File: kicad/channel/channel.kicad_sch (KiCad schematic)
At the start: 34 parts, among them J1 Conn_01x07_Male, J2 Conn_01x01_Male, J3 Conn_01x01_Male, J4 Conn_01x01_Male, J5 Conn_01x01_Male, Q1 BC846B, Q2 IRF3205, Q3 IRF3205, Q4 BC846B, Q5 IRF3205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

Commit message: work on kicad
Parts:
- removed C5, C6: 10u, Capacitor_SMD:CP_Elec_6.3x7.7, symbol Device:C_Polarized
- added C5, C6: 1u, Capacitor_SMD:C_0603_1608Metric, symbol Device:C
- added R17, R18: 10k, Resistor_SMD:R_1206_3216Metric, symbol Device:R
- added R19, R20: 2.2k, Resistor_SMD:R_1206_3216Metric, symbol Device:R
- R10, R11, R2, R3: value 47k -> 22k
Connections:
- net GND: now also R19.1, R20.1; no longer Q1.2 (E), Q4.2 (E)
- net at R1.2, U1.14: now also R18.1
- net at R2.2, R4.1, U1.9 (-): now also C5.1
- net at R9.2, U1.8: now also R17.1
- net at R10.2, R12.1, U1.13 (-): now also C6.1
- new net: C5.2, R17.2
- new net: Q1.2 (E), R19.2
- new net: C6.2, R18.2
- new net: Q4.2 (E), R20.2
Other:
- moved on the sheet: R1, R9, U1C, U1D

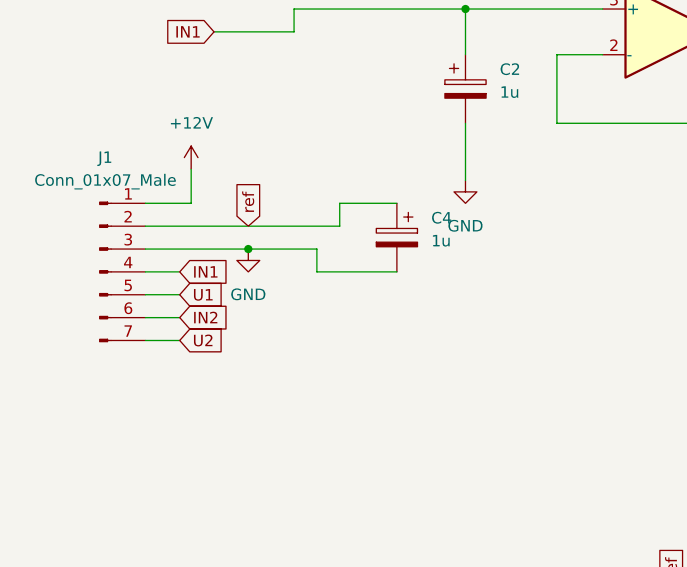
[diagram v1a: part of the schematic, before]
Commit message: rework PINS, get SD Card working
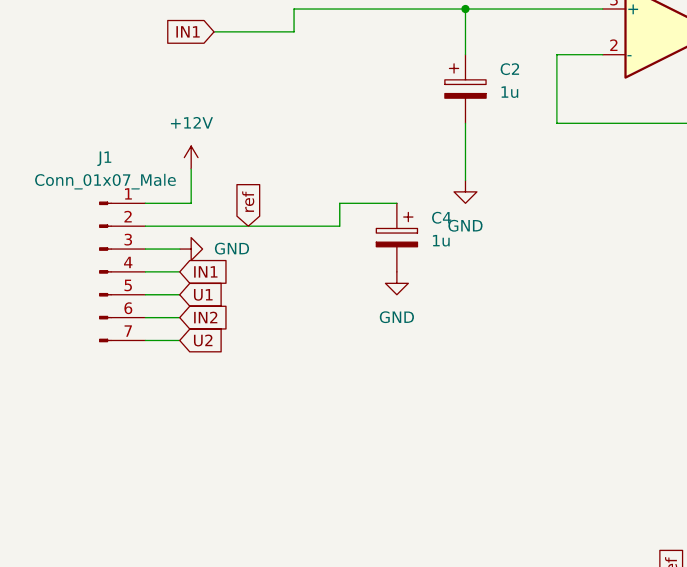
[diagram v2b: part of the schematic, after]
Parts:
- R8: footprint Resistor_THT:R_Axial_DIN0614_L14.3mm_D5.7mm_P25.40mm_Horizontal -> Resistor_THT:R_Axial_DIN0614_L14.3mm_D5.7mm_P20.32mm_Horizontal
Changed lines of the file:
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@@
   (junction (at 152.4 132.08) (diameter 0) (color 0 0 0 0)
   )
-  (junction (at 38.1 97.79) (diameter 0) (color 0 0 0 0)
-  )
   (junction (at 167.64 121.92) (diameter 0) (color 0 0 0 0)
   )
@@
     (stroke (width 0) (type default) (color 0 0 0 0))
   )
-  (wire (pts (xy 45.72 97.79) (xy 45.72 100.33))
-    (stroke (width 0) (type default) (color 0 0 0 0))
-  )
   (wire (pts (xy 153.67 83.82) (xy 153.67 87.63))
     (stroke (width 0) (type default) (color 0 0 0 0))
@@
     (stroke (width 0) (type default) (color 0 0 0 0))
   )
+  (wire (pts (xy 26.67 97.79) (xy 30.48 97.79))
+    (stroke (width 0) (type default) (color 0 0 0 0))
+  )
   (wire (pts (xy 124.46 132.08) (xy 130.81 132.08))
     (stroke (width 0) (type default) (color 0 0 0 0))
@@
     (stroke (width 0) (type default) (color 0 0 0 0))
   )
-  (wire (pts (xy 26.67 97.79) (xy 38.1 97.79))
-    (stroke (width 0) (type default) (color 0 0 0 0))
-  )
   (wire (pts (xy 111.76 144.78) (xy 114.3 144.78))
     (stroke (width 0) (type default) (color 0 0 0 0))
@@
     (stroke (width 0) (type default) (color 0 0 0 0))
   )
-  (wire (pts (xy 45.72 100.33) (xy 54.61 100.33))
-    (stroke (width 0) (type default) (color 0 0 0 0))
-  )
   (wire (pts (xy 54.61 92.71) (xy 48.26 92.71))
     (stroke (width 0) (type default) (color 0 0 0 0))
@@
   )
   (wire (pts (xy 201.93 73.66) (xy 129.54 73.66))
-    (stroke (width 0) (type default) (color 0 0 0 0))
-  )
-  (wire (pts (xy 38.1 97.79) (xy 45.72 97.79))
     (stroke (width 0) (type default) (color 0 0 0 0))
   )
@@
     (pin "1")
   )
+  (symbol (lib_id "power:GND") (at 30.48 97.79 90) (unit 1)
+    (in_bom yes) (on_board yes) (fields_autoplaced)
+    (property "Reference" "#PWR0105" (id 0) (at 36.83 97.79 0)
+      (effects (font (size 1.27 1.27)) hide)
+    )
+    (property "Value" "GND" (id 1) (at 34.29 97.7899 90)
+      (effects (font (size 1.27 1.27)) (justify right))
+    )
+    (property "Footprint" "" (id 2) (at 30.48 97.79 0)
+      (effects (font (size 1.27 1.27)) hide)
+    )
+    (property "Datasheet" "" (id 3) (at 30.48 97.79 0)
+      (effects (font (size 1.27 1.27)) hide)
+    )
+    (pin "1")
+  )
   (symbol (lib_id "power:GND") (at 154.94 163.83 0) (unit 1)
     (in_bom yes) (on_board yes) (fields_autoplaced)
@@
     (pin "2")
   )
-  (symbol (lib_id "power:GND") (at 38.1 97.79 0) (unit 1)
-    (in_bom yes) (on_board yes) (fields_autoplaced)
-    (property "Reference" "#PWR0103" (id 0) (at 38.1 104.14 0)
-      (effects (font (size 1.27 1.27)) hide)
-    )
-    (property "Value" "GND" (id 1) (at 38.1 102.87 0))
-    (property "Footprint" "" (id 2) (at 38.1 97.79 0)
-      (effects (font (size 1.27 1.27)) hide)
-    )
-    (property "Datasheet" "" (id 3) (at 38.1 97.79 0)
+  (symbol (lib_id "power:GND") (at 54.61 100.33 0) (unit 1)
+    (in_bom yes) (on_board yes) (fields_autoplaced)
+    (property "Reference" "#PWR0103" (id 0) (at 54.61 106.68 0)
+      (effects (font (size 1.27 1.27)) hide)
+    )
+    (property "Value" "GND" (id 1) (at 54.61 105.41 0))
+    (property "Footprint" "" (id 2) (at 54.61 100.33 0)
+      (effects (font (size 1.27 1.27)) hide)
+    )
+    (property "Datasheet" "" (id 3) (at 54.61 100.33 0)
       (effects (font (size 1.27 1.27)) hide)
     )
@@
     (property "Reference" "R8" (id 0) (at 182.88 115.57 90))
     (property "Value" "0.22" (id 1) (at 182.88 118.11 90))
-    (property "Footprint" "Resistor_THT:R_Axial_DIN0614_L14.3mm_D5.7mm_P25.40mm_Horizontal" (id 2) (at 182.88 123.698 90)
+    (property "Footprint" "Resistor_THT:R_Axial_DIN0614_L14.3mm_D5.7mm_P20.32mm_Horizontal" (id 2) (at 182.88 123.698 90)
       (effects (font (size 1.27 1.27)) hide)
     )
@@
       (reference "#PWR0104") (unit 1) (value "+12V") (footprint "")
     )
+    (path "/8a8f424c-3033-4534-9311-6e7b42dedc1f"
+      (reference "#PWR0105") (unit 1) (value "GND") (footprint "")
+    )
     (path "/98bcbe84-6de1-4d54-8e02-faa40f5f06a1"
       (reference "C1") (unit 1) (value "1u") (footprint "Capacitor_SMD:C_0603_1608Metric")
@@
     )
     (path "/c800057a-d278-4182-854b-774312f90617"
-      (reference "R8") (unit 1) (value "0.22") (footprint "Resistor_THT:R_Axial_DIN0614_L14.3mm_D5.7mm_P25.40mm_Horizontal")
+      (reference "R8") (unit 1) (value "0.22") (footprint "Resistor_THT:R_Axial_DIN0614_L14.3mm_D5.7mm_P20.32mm_Horizontal")
     )
     (path "/5f4f5dfc-c04c-423a-8bfb-e97fdc53c047"

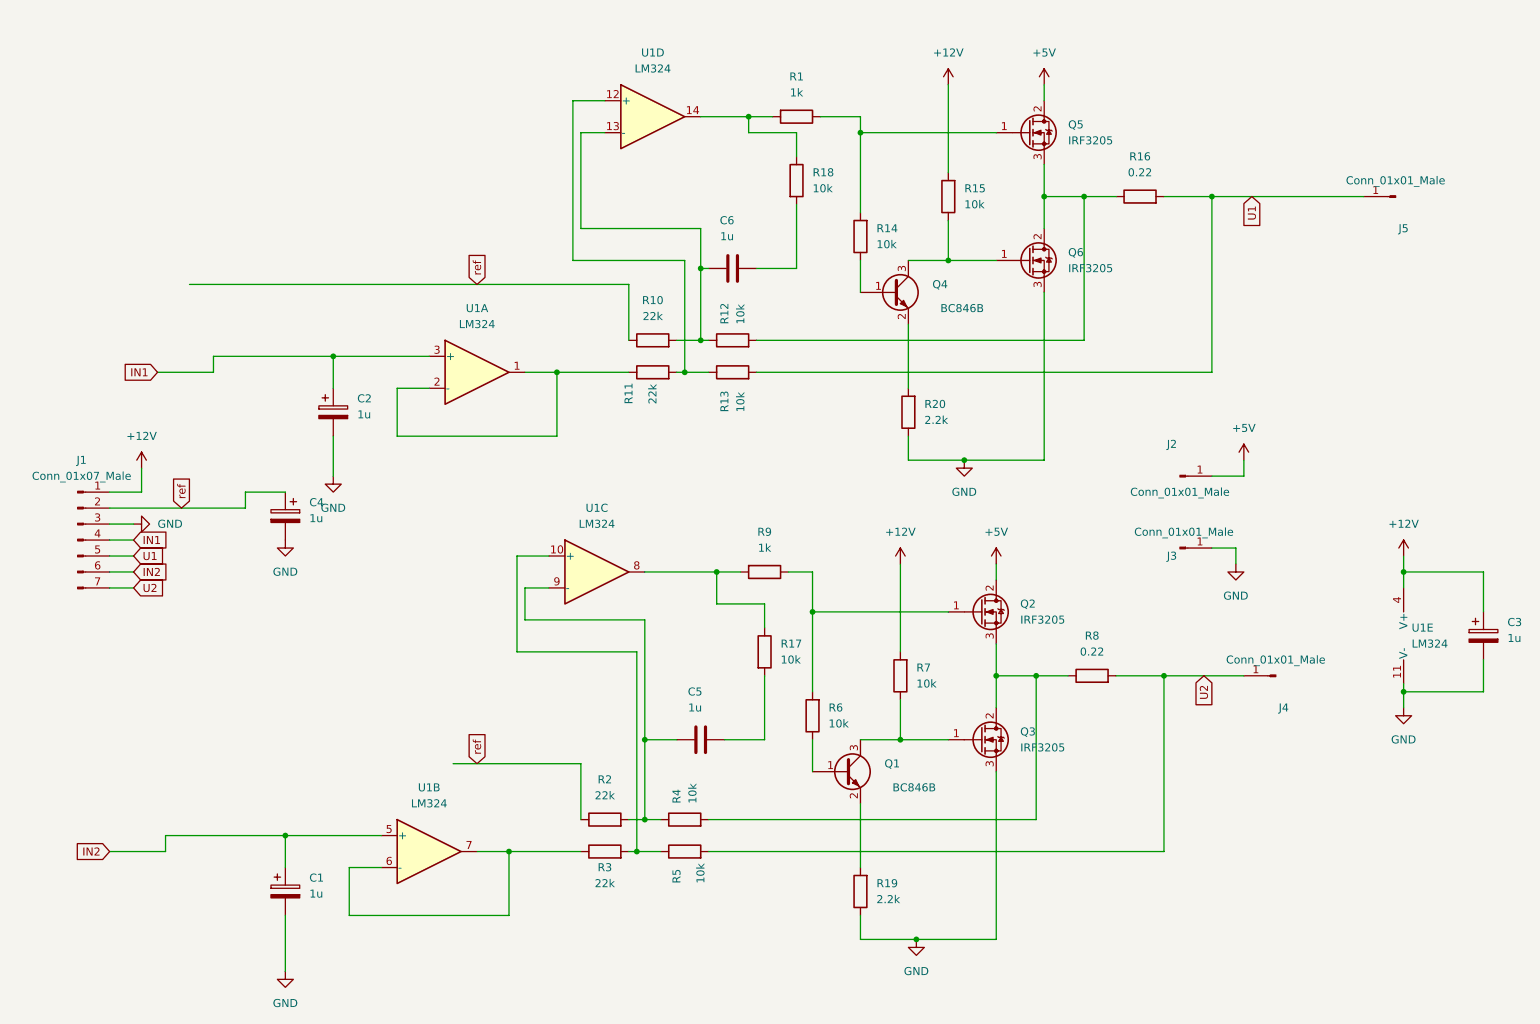
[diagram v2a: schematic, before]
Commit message: fix flash, fix frequency compensation
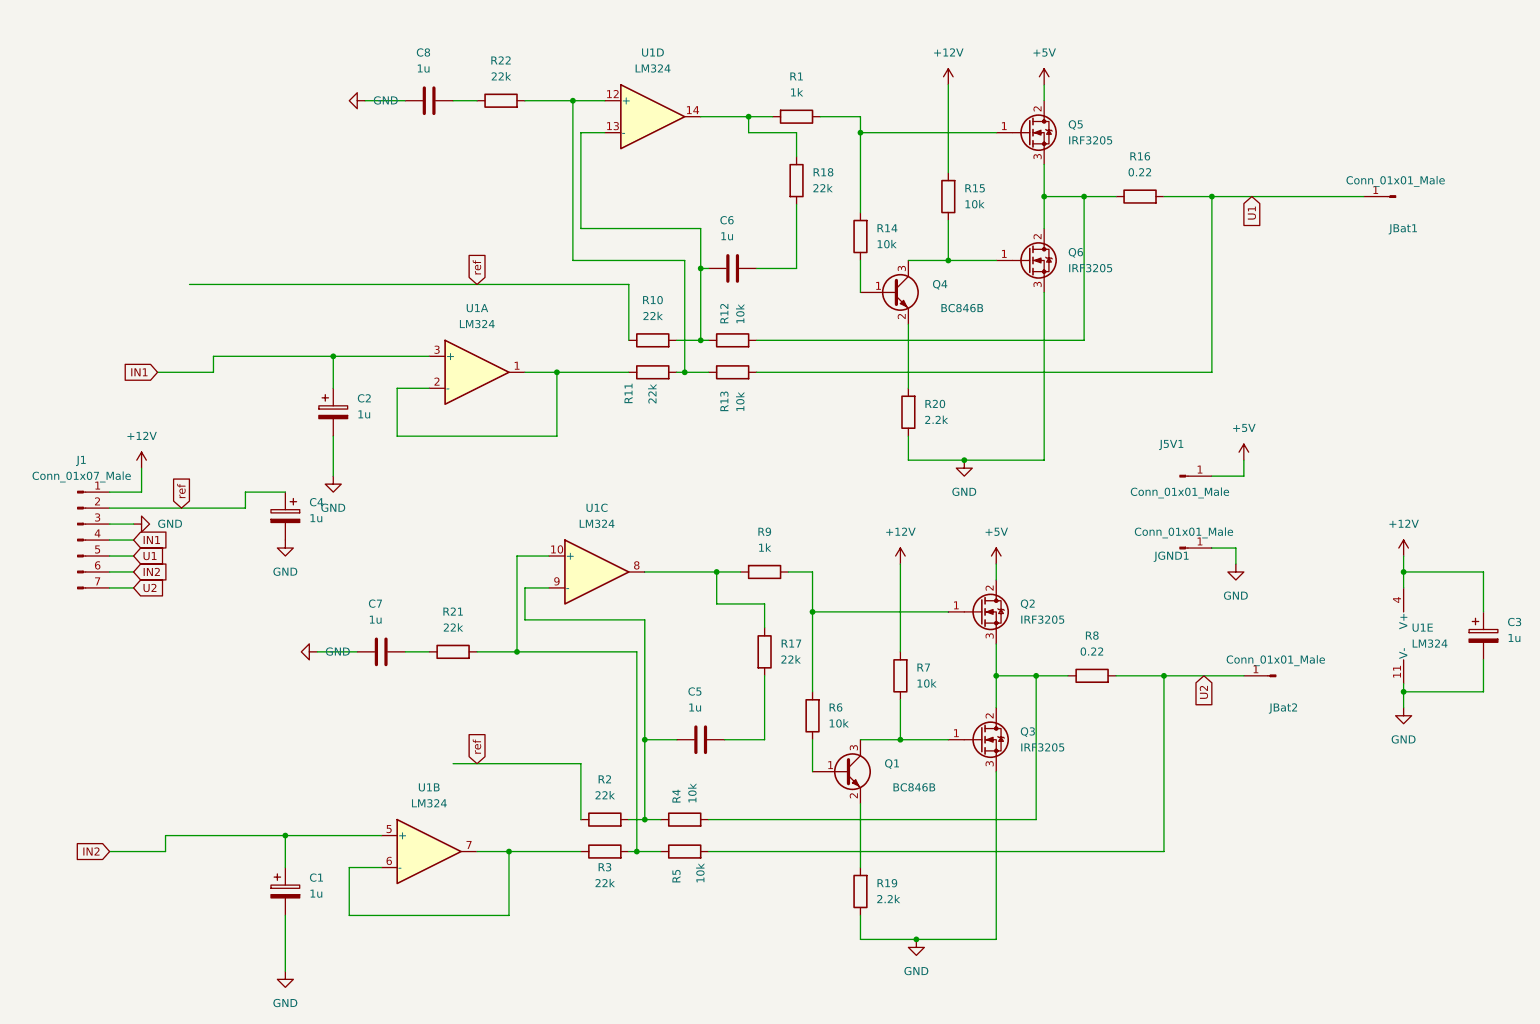
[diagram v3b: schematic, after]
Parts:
- added C7, C8: 1u, Capacitor_SMD:C_0603_1608Metric, symbol Device:C
- added R21, R22: 22k, Resistor_SMD:R_1206_3216Metric, symbol Device:R
- J5V1: renamed from J2; footprint Connector_Pin:Pin_D1.3mm_L11.0mm -> Channel:PowerPad
- JBat1: renamed from J5; footprint Connector_Pin:Pin_D1.3mm_L11.0mm -> Channel:PowerPad
- JBat2: renamed from J4; footprint Connector_Pin:Pin_D1.3mm_L11.0mm -> Channel:PowerPad
- JGND1: renamed from J3; footprint Connector_Pin:Pin_D1.3mm_L11.0mm -> Channel:PowerPad
- R16, R8: footprint Resistor_THT:R_Axial_DIN0614_L14.3mm_D5.7mm_P20.32mm_Horizontal -> Resistor_THT:R_Axial_DIN0617_L17.0mm_D6.0mm_P25.40mm_Horizontal
- R17, R18: value 10k -> 22k
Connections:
- net GND: now also C7.1, C8.1
- net at R11.2, R13.1, U1.12 (+): now also R22.2
- net at R3.2, R5.1, U1.10 (+): now also R21.2
- new net: C7.2, R21.1
- new net: C8.2, R22.1

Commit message: add resistor matching
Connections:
- net at R17.1, R9.2, U1.8: now also R6.2
- net at Q5.1 (G), R1.1: no longer R14.2
- net at R1.2, R18.1, U1.14: now also R14.2
- net at Q2.1 (G), R9.1: no longer R6.2
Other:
- moved on the sheet: Q2, Q5, R1, R9
